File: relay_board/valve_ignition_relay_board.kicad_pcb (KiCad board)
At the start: 4 copper layers, 63.8 x 103.9 mm, 100 parts, among them J1 Programming Header, J2 ACT_PWR, J3 ACT_PWR, J4 Actuator, J5 CAN Connector Left, J6 CAN Connector Right, K1 PS2702-1-F3-A, K2 PS2702-1-F3-A, K3 T9GV1L14-12, K4 T92S11D12-12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

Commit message: Silkscreen extras
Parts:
- TP1, TP2, TP3, TP4: moved to F.Cu
- turned TP1 to 0 degrees
- turned TP2 to 0 degrees
- turned TP3 to 0 degrees
- turned TP4 to 0 degrees
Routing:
- net /DipSwitch/~{MCLR}: track 25.8 -> 27.0 mm, vias 1 -> 2
- net GND: vias 102 -> 141
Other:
- board text added: "+12V"
- board text added: "+5V"
- board text added: "+BATT"
- board text added: "1"
- board text added: "12V"
- board text added: "2"
- board text added: "3"
- board text added: "4"
- board text added: "5"
- board text added: "5V"
- board text added: "6"
- board text added: "BAT"
- board text added: "CANH"
- board text added: "CANL"
- board text added: "GND"

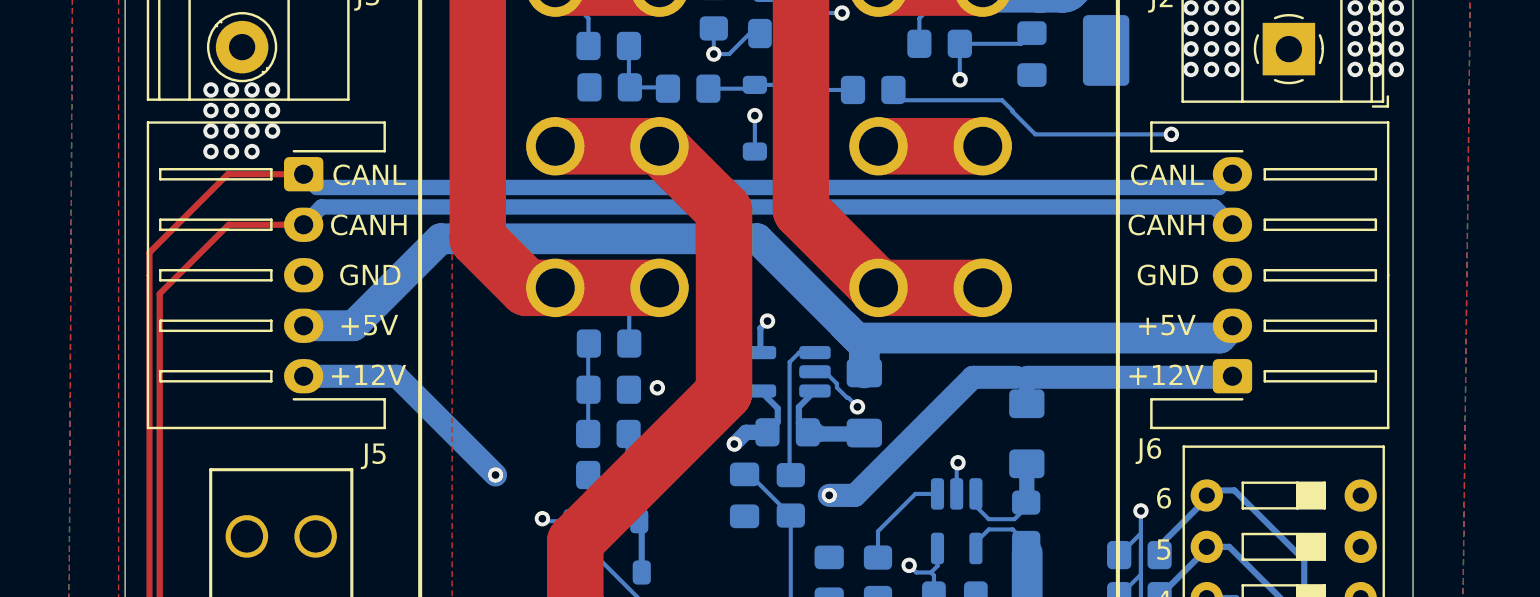
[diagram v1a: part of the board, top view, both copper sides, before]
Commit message: Push JSTs to board edge
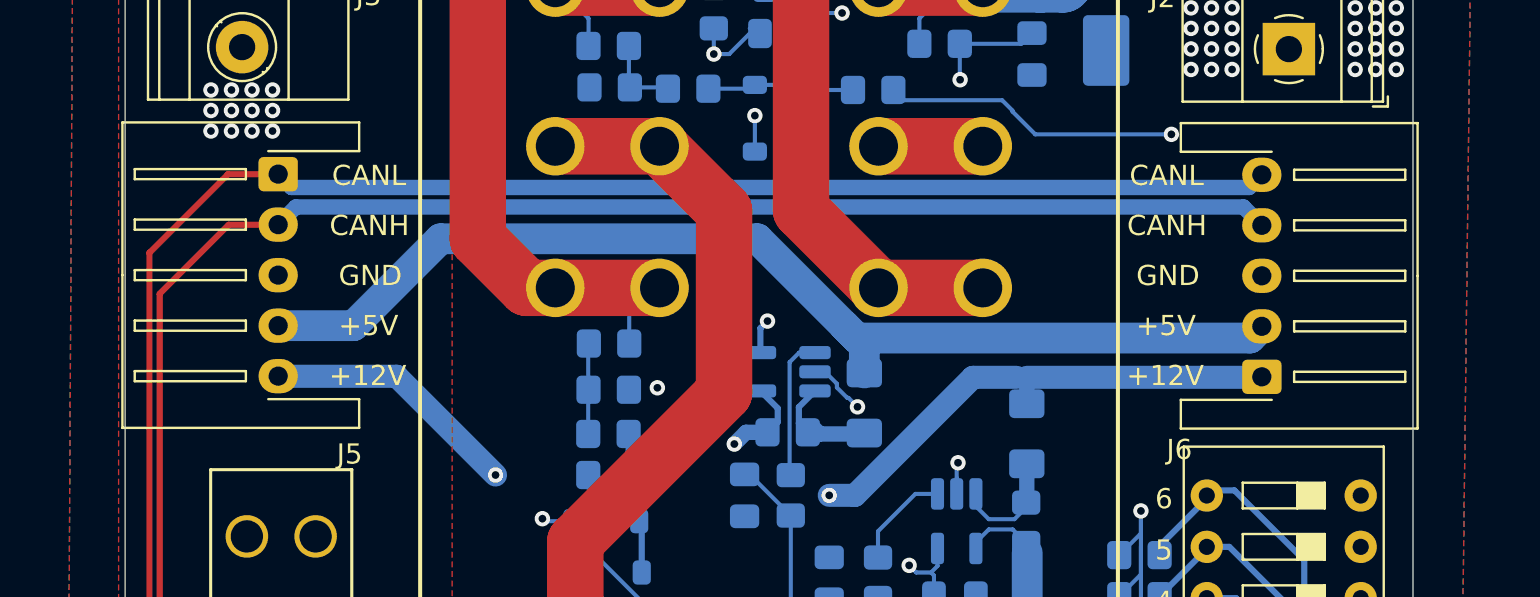
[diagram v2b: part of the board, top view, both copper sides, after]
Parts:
- moved J6 1.46 mm to (150.8, 65.8)
- moved J5 1.26 mm to (102.1, 55.7)
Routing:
- net Net-(J5-Pin_5): track 51.7 -> 54.4 mm
- net Net-(J5-Pin_4): track 52.8 -> 55.5 mm
- net /DipSwitch/CANH: track 145.6 -> 147.0 mm
- net /DipSwitch/CANL: track 148.6 -> 150.1 mm
- net GND: vias 141 -> 138
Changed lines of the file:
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@@
 	(footprint "Connector_JST:JST_XH_S5B-XH-A-1_1x05_P2.50mm_Horizontal"
 		(layer "F.Cu")
-		(at 149.370362 65.7332 90)
+		(at 150.8252 65.7606 90)
 		(descr "JST XH series connector, S5B-XH-A-1 (http://www.jst-mfg.com/product/pdf/eng/eXH.pdf), generated with kicad-footprint-generator")
 		(tags "connector JST XH horizontal")
@@
 	(footprint "Connector_JST:JST_XH_S5B-XH-A-1_1x05_P2.50mm_Horizontal"
 		(layer "F.Cu")
-		(at 103.396362 55.7332 -90)
+		(at 102.1334 55.7276 -90)
 		(descr "JST XH series connector, S5B-XH-A-1 (http://www.jst-mfg.com/product/pdf/eng/eXH.pdf), generated with kicad-footprint-generator")
 		(tags "connector JST XH horizontal")
@@
 		(height 29.591)
 		(orientation 1)
-		(gr_text "3500.0000 mils"
+		(gr_text "88.9000 mm"
 			(at 165.982 81.026 90)
 			(layer "User.1")
@@
 		(height -17.779)
 		(orientation 0)
-		(gr_text "2000.0000 mils"
+		(gr_text "50.8000 mm"
 			(at 125.095 17.646 0)
 			(layer "User.1")
@@
 	)
 	(via
-		(at 98.806 54.61)
-		(size 0.762)
-		(drill 0.381)
-		(layers "F.Cu" "B.Cu")
-		(free yes)
-		(net 1)
-	)
-	(via
 		(at 151.158822 118.901278)
 		(size 0.762)
@@
 	)
 	(via
-		(at 99.822 54.61)
-		(size 0.762)
-		(drill 0.381)
-		(layers "F.Cu" "B.Cu")
-		(free yes)
-		(net 1)
-	)
-	(via
 		(at 121.158 86.868)
 		(size 0.762)
@@
 	)
 	(via
-		(at 100.838 54.61)
-		(size 0.762)
-		(drill 0.381)
-		(layers "F.Cu" "B.Cu")
-		(free yes)
-		(net 1)
-	)
-	(via
 		(at 156.492822 113.567278)
 		(size 0.762)
@@
 	)
 	(segment
-		(start 103.396362 63.2332)
-		(end 105.859424 63.2332)
-		(width 1.524)
-		(layer "B.Cu")
-		(net 13)
-	)
-	(segment
 		(start 110.164624 58.928)
 		(end 125.8594 58.928)
@@
 	)
 	(segment
-		(start 130.1653 63.2339)
-		(end 130.772299 63.840899)
+		(start 102.1334 63.2276)
+		(end 105.865024 63.2276)
 		(width 1.524)
 		(layer "B.Cu")
@@
 	)
 	(segment
-		(start 148.762663 63.840899)
-		(end 149.370362 63.2332)
+		(start 130.772299 63.840899)
+		(end 150.244901 63.840899)
 		(width 1.524)
 		(layer "B.Cu")
@@
 	)
 	(segment
-		(start 130.772299 63.840899)
-		(end 148.762663 63.840899)
+		(start 150.244901 63.840899)
+		(end 150.8252 63.2606)
 		(width 1.524)
 		(layer "B.Cu")
@@
 	)
 	(segment
-		(start 105.859424 63.2332)
+		(start 105.865024 63.2276)
 		(end 110.164624 58.928)
 		(width 1.524)
@@
 	)
 	(segment
+		(start 130.1653 63.2339)
+		(end 130.772299 63.840899)
+		(width 1.524)
+		(layer "B.Cu")
+		(net 13)
+	)
+	(segment
 		(start 128.3553 68.5084)
 		(end 127.9077 68.0608)
@@
 	)
 	(segment
+		(start 150.7998 65.786)
+		(end 150.8252 65.7606)
+		(width 1.143)
+		(layer "B.Cu")
+		(net 15)
+	)
+	(segment
 		(start 139.192 65.786)
-		(end 149.317562 65.786)
+		(end 150.7998 65.786)
 		(width 1.143)
 		(layer "B.Cu")
@@
 	)
 	(segment
-		(start 149.317562 65.786)
-		(end 149.370362 65.7332)
+		(start 108.0053 65.7332)
+		(end 102.139 65.7332)
 		(width 1.143)
 		(layer "B.Cu")
@@
 	)
 	(segment
-		(start 108.0053 65.7332)
-		(end 103.396362 65.7332)
-		(width 1.143)
+		(start 139.192 67.0925)
+		(end 139.192 65.786)
+		(width 0.762)
 		(layer "B.Cu")
 		(net 15)
 	)
 	(segment
-		(start 112.8933 70.6212)
-		(end 108.0053 65.7332)
+		(start 136.525 65.786)
+		(end 138.684 65.786)
 		(width 1.143)
 		(layer "B.Cu")
@@
 	)
 	(segment
-		(start 139.192 67.0925)
-		(end 139.192 65.786)
-		(width 0.762)
+		(start 112.8933 70.6212)
+		(end 108.0053 65.7332)
+		(width 1.143)
 		(layer "B.Cu")
 		(net 15)
 	)
 	(segment
-		(start 136.525 65.786)
-		(end 138.684 65.786)
+		(start 102.139 65.7332)
+		(end 102.1334 65.7276)
 		(width 1.143)
 		(layer "B.Cu")
@@
 	)
 	(segment
-		(start 107.395584 127.787422)
-		(end 105.121638 125.513476)
+		(start 121.380428 127.787422)
+		(end 107.395584 127.787422)
 		(width 0.3048)
 		(layer "F.Cu")
@@
 	)
 	(segment
-		(start 125.476 124.206)
-		(end 124.96185 124.206)
+		(start 124.96185 124.206)
+		(end 121.380428 127.787422)
+		(width 0.3048)
+		(layer "F.Cu")
+		(net 25)
+	)
+	(segment
+		(start 107.395584 127.787422)
+		(end 105.121638 125.513476)
 		(width 0.3048)
 		(layer "F.Cu")
@@
 	(segment
 		(start 99.683424 58.2332)
-		(end 103.396362 58.2332)
+		(end 102.1278 58.2332)
 		(width 0.3048)
 		(layer "F.Cu")
@@
 	)
 	(segment
-		(start 105.121638 125.513476)
-		(end 105.121638 121.885638)
+		(start 125.476 124.206)
+		(end 124.96185 124.206)
 		(width 0.3048)
 		(layer "F.Cu")
@@
 	)
 	(segment
-		(start 121.380428 127.787422)
-		(end 107.395584 127.787422)
+		(start 105.121638 125.513476)
+		(end 105.121638 121.885638)
 		(width 0.3048)
 		(layer "F.Cu")
@@
 	)
 	(segment
-		(start 124.96185 124.206)
-		(end 121.380428 127.787422)
+		(start 102.1278 58.2332)
+		(end 102.1334 58.2276)
 		(width 0.3048)
 		(layer "F.Cu")
@@
 	)
 	(segment
-		(start 103.396362 58.2332)
-		(end 104.276362 57.3532)
+		(start 103.0078 57.3532)
+		(end 149.9178 57.3532)
 		(width 0.762)
 		(layer "B.Cu")
@@
 	)
 	(segment
-		(start 148.490362 57.3532)
-		(end 149.370362 58.2332)
+		(start 102.1334 58.2276)
+		(end 103.0078 57.3532)
 		(width 0.762)
 		(layer "B.Cu")
@@
 	)
 	(segment
-		(start 104.276362 57.3532)
-		(end 148.490362 57.3532)
+		(start 149.9178 57.3532)
+		(end 150.8252 58.2606)
 		(width 0.762)
 		(layer "B.Cu")
@@
 	)
 	(segment
-		(start 99.643424 55.7332)
-		(end 103.396362 55.7332)
+		(start 102.1278 55.7332)
+		(end 102.1334 55.7276)
 		(width 0.3048)
 		(layer "F.Cu")
@@
 	)
 	(segment
-		(start 124.41027 125.476)
-		(end 121.590848 128.295422)
+		(start 121.590848 128.295422)
+		(end 107.185164 128.295422)
 		(width 0.3048)
 		(layer "F.Cu")
@@
 	)
 	(segment
-		(start 104.613638 125.723896)
-		(end 104.613638 122.139638)
+		(start 99.643424 55.7332)
+		(end 102.1278 55.7332)
 		(width 0.3048)
 		(layer "F.Cu")
@@
 	)
 	(segment
-		(start 121.590848 128.295422)
-		(end 107.185164 128.295422)
+		(start 104.613638 125.723896)
+		(end 104.613638 122.139638)
 		(width 0.3048)
 		(layer "F.Cu")
@@
 	)
 	(segment
-		(start 107.185164 128.295422)
-		(end 104.613638 125.723896)
+		(start 95.758 59.618624)
+		(end 99.643424 55.7332)
 		(width 0.3048)
 		(layer "F.Cu")
@@
 	)
 	(segment
-		(start 95.758 59.618624)
-		(end 99.643424 55.7332)
+		(start 107.185164 128.295422)
+		(end 104.613638 125.723896)
 		(width 0.3048)
 		(layer "F.Cu")
@@
 	)
 	(segment
-		(start 95.758 113.284)
-		(end 95.758 59.618624)
+		(start 124.41027 125.476)
+		(end 121.590848 128.295422)
 		(width 0.3048)
 		(layer "F.Cu")
@@
 	)
 	(segment
-		(start 103.396362 55.7332)
-		(end 104.051162 56.388)
+		(start 95.758 113.284)
+		(end 95.758 59.618624)
+		(width 0.3048)
+		(layer "F.Cu")
+		(net 26)
+	)
+	(segment
+		(start 150.1978 56.388)
+		(end 150.8252 55.7606)
 		(width 0.762)
 		(layer "B.Cu")
@@
 	)
 	(segment
-		(start 148.715562 56.388)
-		(end 149.370362 55.7332)
+		(start 102.7938 56.388)
+		(end 150.1978 56.388)
 		(width 0.762)
 		(layer "B.Cu")
@@
 	)
 	(segment
-		(start 104.051162 56.388)
-		(end 148.715562 56.388)
+		(start 102.1334 55.7276)
+		(end 102.7938 56.388)
 		(width 0.762)
 		(layer "B.Cu")

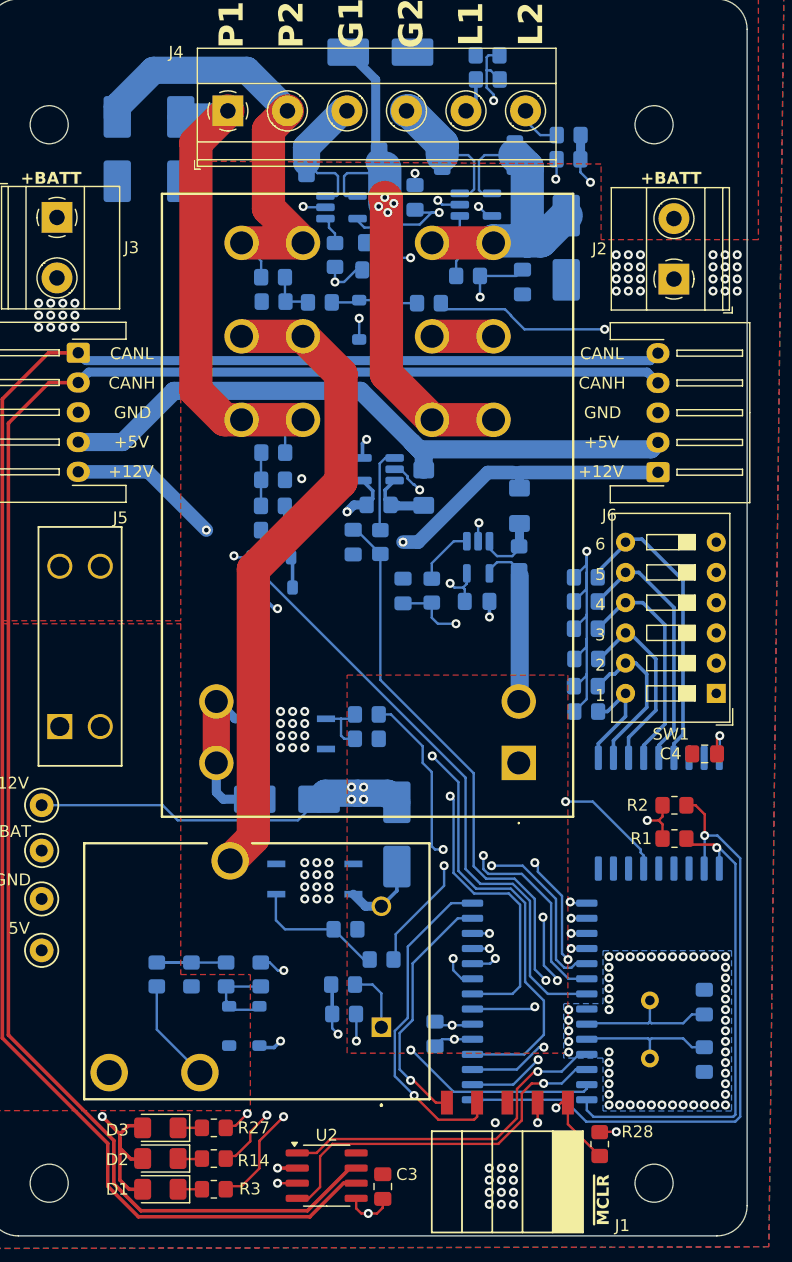
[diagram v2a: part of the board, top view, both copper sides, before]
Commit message: tidy up traces, add board name silkscreen
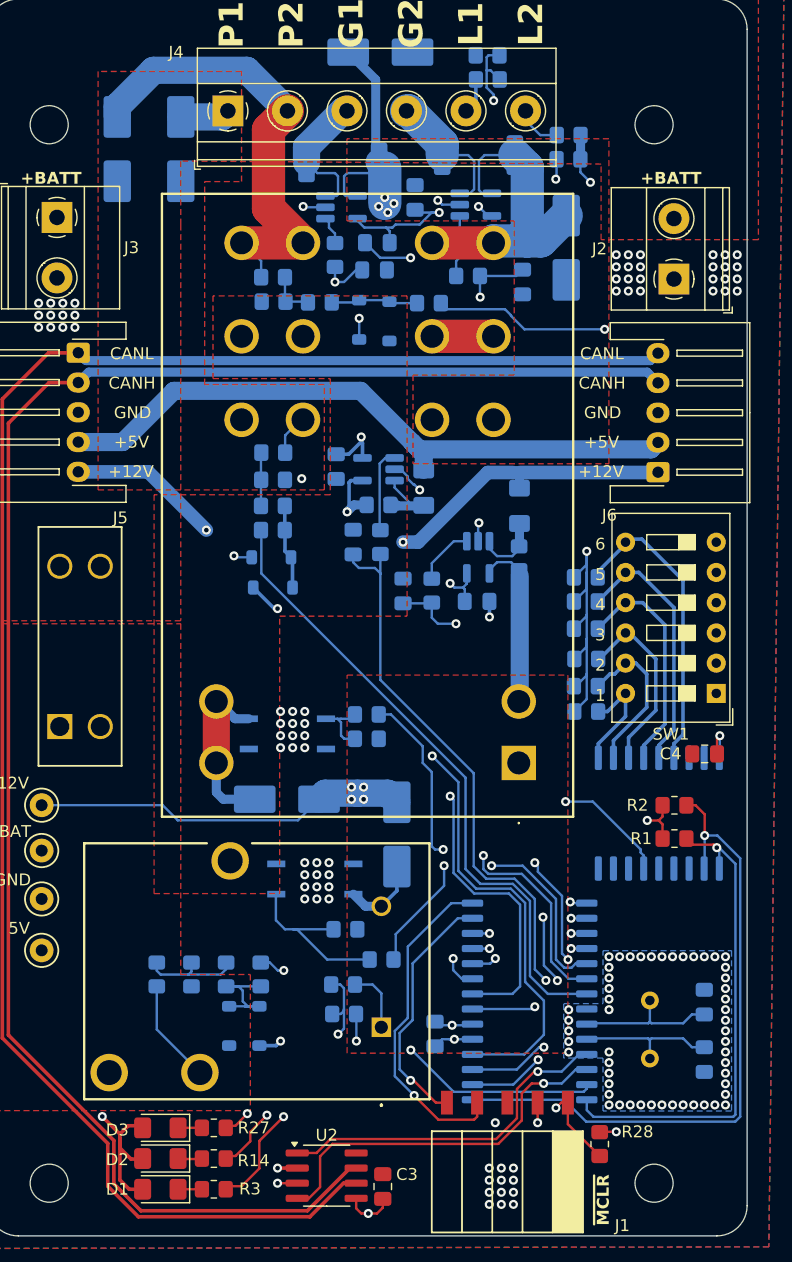
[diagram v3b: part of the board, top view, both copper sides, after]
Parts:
- turned C13 to -90 degrees
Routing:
- net /Relay/T92S11D12-12/COM1: track 54.4 -> 0.00 mm
- net /Relay/P1: track 42.3 -> 7.69 mm
- net /Relay/T92S11D12-12/NC2: track 45.6 -> 19.7 mm
- net Net-(K1-Pad1): track 11.4 -> 14.8 mm
- net GND: track 32.9 -> 30.6 mm, vias 138 -> 137
- net /DipSwitch/VSENSE_12V: track 28.5 -> 30.4 mm
- net +12V: track 52.5 -> 50.8 mm
- net Net-(J4-Pin_6): track 4.65 -> 3.13 mm
- net Net-(U11-IN+): track 6.33 -> 4.88 mm
- net Net-(U10-IN+): track 5.62 -> 6.92 mm
- net /DipSwitch/SCL: track 42.6 -> 41.6 mm
- net /DipSwitch/DIP_6: track 25.5 -> 24.5 mm
- net Net-(D12-K): track 7.39 -> 8.27 mm
- net /DipSwitch/CAN_TX: track 29.2 -> 28.4 mm
- net Net-(D10-K): track 7.31 -> 6.48 mm
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- added copper zone on F.Cu, net /Relay/P1
- added copper zone on F.Cu, net /Relay/T92S11D12-12/COM1
- added copper zone on F.Cu, net /Relay/T92S11D12-12/NC2

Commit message: add team logo
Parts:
- added G***: LOGO, Team_Logo:Logo_SilkScreen_10mm, B.Cu at (125.5, 119.8)
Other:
- board text added: "Unified Relay Board Joelle G, Joe D, Ash L 09/2025"
